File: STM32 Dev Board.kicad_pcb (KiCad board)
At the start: 2 copper layers, 38.5 x 32.7 mm, 36 parts, among them J5 2 Pin JST, J6 USB_B_Micro, Q1 PMOS, U1 MCP2221A-I/ML, U2 STM32F070F6Px, U3 MCP1824S, U4 MCP73113

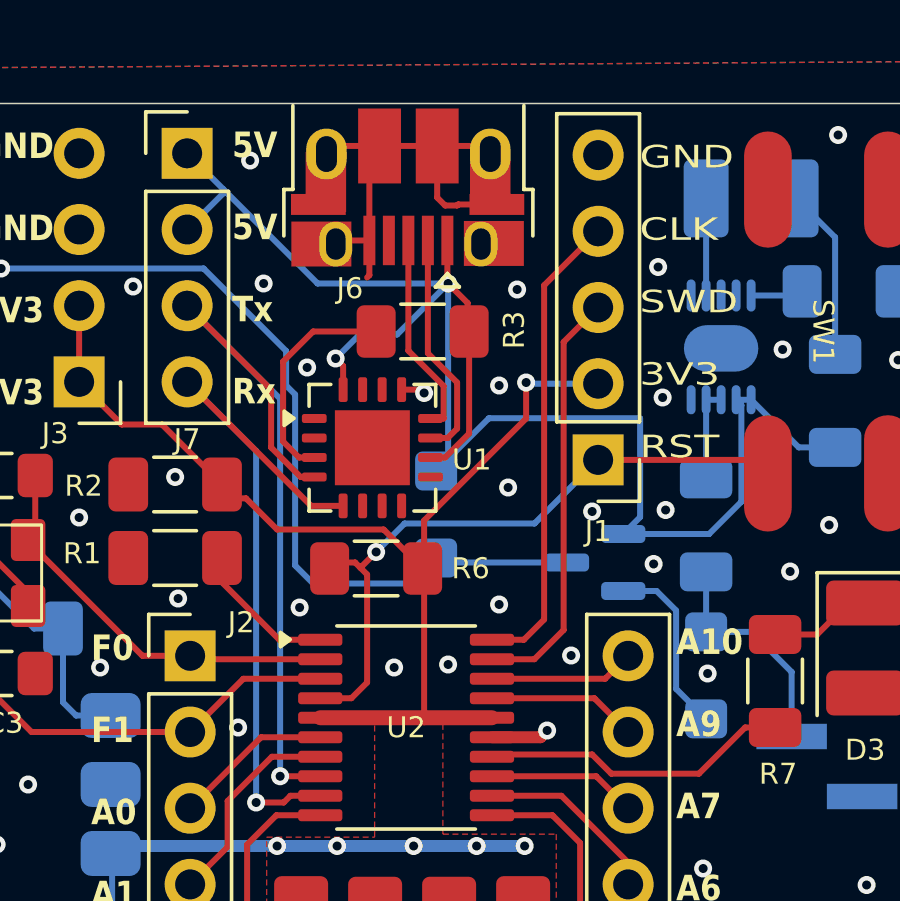
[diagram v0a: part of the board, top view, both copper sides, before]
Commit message: changed power supply of USB to UART to match datasheet, added changes to pcb Signed-off-by: Fozface <tyler.hickling99@gmail.com>
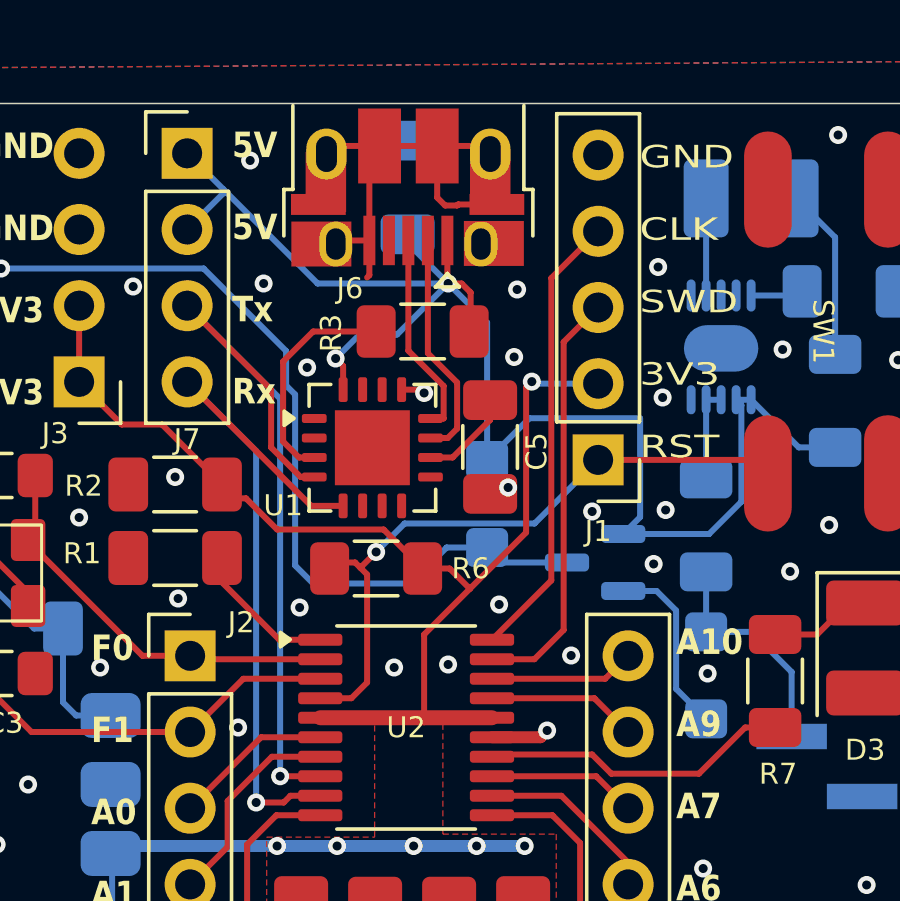
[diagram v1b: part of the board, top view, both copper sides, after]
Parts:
- added C10: 5u, Capacitor_SMD:C_1206_3216Metric_Pad1.33x1.80mm_HandSolder, B.Cu at (141.3, 68.8)
- added C5: 0.22-0.47u, Capacitor_SMD:C_1206_3216Metric_Pad1.33x1.80mm_HandSolder, F.Cu at (144.1, 77.5)
- moved D2 1.74 mm to (144.0, 79.3)
- turned R3 to 0 degrees
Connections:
- net +3.3V renamed 3.3V
- R3 pad 1: VUSB -> Net-(U1-~{RST})
- R3 pad 2: Net-(U1-~{RST}) -> VUSB
- U1 pad 10: VUSB -> Net-(U1-VUSB)
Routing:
- net VUSB: track 56.6 -> 52.4 mm
- net Net-(U1-VUSB): track 0.00 -> 3.17 mm
- net 3.3V: track 53.5 -> 55.2 mm
- net /MCU/SWCLK: track 15.7 -> 15.1 mm

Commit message: repour ground on pcb
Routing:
- net 3.3V: track 55.2 -> 56.1 mm
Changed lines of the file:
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@@
 	)
 	(via
-		(at 144.9 74.45)
+		(at 144.75 74.15)
 		(size 0.6)
 		(drill 0.3)
@@
 	)
 	(segment
-		(start 146.140118 71.819882)
+		(start 146.1 71.86)
 		(end 147.7 70.26)
 		(width 0.2)
@@
 	)
 	(segment
-		(start 146.140118 81.897382)
-		(end 146.140118 71.819882)
+		(start 144.975 83.875)
+		(end 146.1 82.75)
 		(width 0.2)
 		(layer "F.Cu")
@@
 	(segment
 		(start 144.1625 83.875)
-		(end 146.140118 81.897382)
+		(end 144.975 83.875)
 		(width 0.2)
 		(layer "F.Cu")
 		(net 3)
+	)
+	(segment
+		(start 146.1 82.75)
+		(end 146.1 71.86)
+		(width 0.2)
+		(layer "F.Cu")
+		(net 3)
+	)
+	(segment
+		(start 146.55 83.55)
+		(end 145.575 84.525)
+		(width 0.2)
+		(layer "F.Cu")
+		(net 4)
+	)
+	(segment
+		(start 147.7 72.8)
+		(end 146.55 73.95)
+		(width 0.2)
+		(layer "F.Cu")
+		(net 4)
 	)
 	(segment
@@
 		(start 146.55 73.95)
 		(end 146.55 83.55)
-		(width 0.2)
-		(layer "F.Cu")
-		(net 4)
-	)
-	(segment
-		(start 146.55 83.55)
-		(end 145.575 84.525)
-		(width 0.2)
-		(layer "F.Cu")
-		(net 4)
-	)
-	(segment
-		(start 147.7 72.8)
-		(end 146.55 73.95)
 		(width 0.2)
 		(layer "F.Cu")
@@
 	)
 	(segment
-		(start 143.425 82.175)
-		(end 145.3 80.3)
+		(start 145.35 80.25)
+		(end 145.35 74.75)
 		(width 0.2)
 		(layer "F.Cu")
@@
 	)
 	(segment
-		(start 145.3 80.3)
-		(end 145.3 75.460869)
-		(width 0.2)
-		(layer "F.Cu")
-		(net 48)
-	)
-	(segment
 		(start 141.85 81.5)
 		(end 140.55 80.2)
@@
 	)
 	(segment
-		(start 145.3 75.460869)
-		(end 145.490118 75.270751)
-		(width 0.2)
-		(layer "F.Cu")
-		(net 48)
-	)
-	(segment
 		(start 140.55 80.2)
 		(end 137 80.2)
@@
 	)
 	(segment
+		(start 143.425 82.175)
+		(end 145.35 80.25)
+		(width 0.2)
+		(layer "F.Cu")
+		(net 48)
+	)
+	(segment
 		(start 135.625 79.1625)
 		(end 133.1625 76.7)
@@
 	)
 	(via
-		(at 145.490118 75.270751)
+		(at 145.35 74.75)
 		(size 0.6)
 		(drill 0.3)
@@
 		(layers "F.Cu" "B.Cu")
 		(free yes)
-		(net 48)
-	)
-	(segment
-		(start 147.7 75.34)
-		(end 145.559367 75.34)
-		(width 0.2)
-		(layer "B.Cu")
 		(net 48)
 	)
@@
 		(start 131.5 93.2375)
 		(end 131.5 91.05)
+		(width 0.2)
+		(layer "B.Cu")
+		(net 48)
+	)
+	(segment
+		(start 145.94 75.34)
+		(end 145.35 74.75)
 		(width 0.2)
 		(layer "B.Cu")
@@
 	)
 	(segment
+		(start 147.7 75.34)
+		(end 145.94 75.34)
+		(width 0.2)
+		(layer "B.Cu")
+		(net 48)
+	)
+	(segment
 		(start 131.571 90.879)
 		(end 131.7 90.75)
@@
 		(layer "B.Cu")
 		(net 48)
-	)
-	(segment
-		(start 145.559367 75.34)
-		(end 145.490118 75.270751)
-		(width 0.2)
-		(layer "B.Cu")
-		(net 48)
